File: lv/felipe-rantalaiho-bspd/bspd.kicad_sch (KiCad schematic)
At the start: 6 parts, among them J1 Conn_01x02, U4 L7805

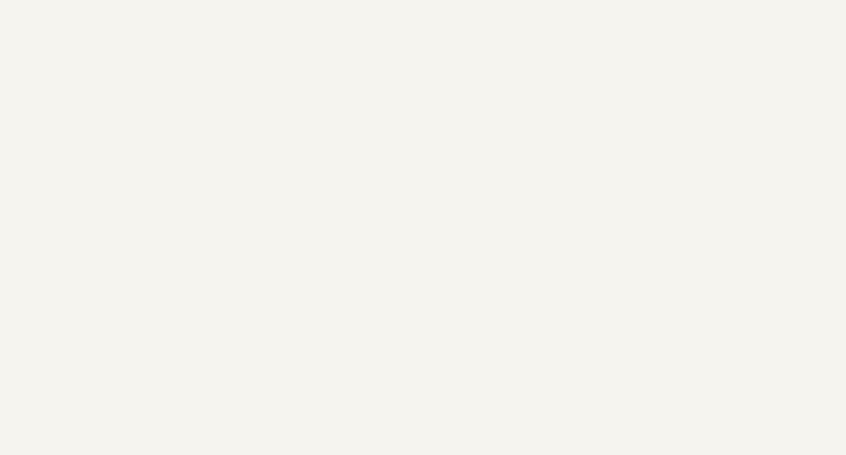
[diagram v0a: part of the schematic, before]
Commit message: Add block 2: brake pressure input + RC filter
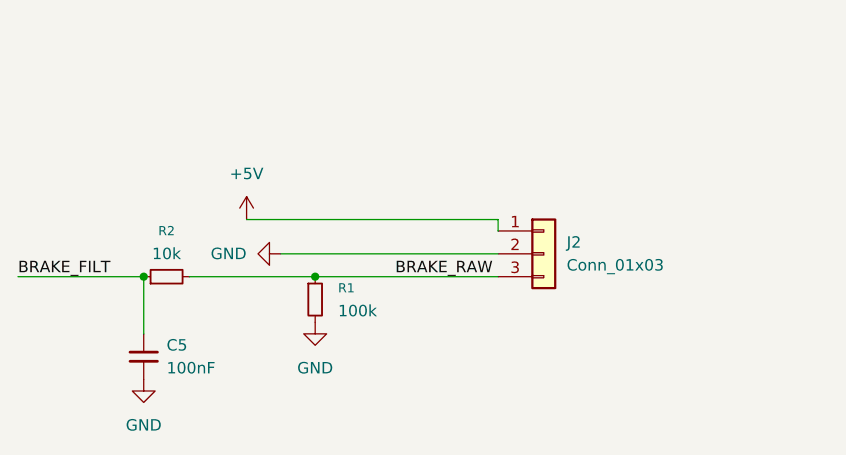
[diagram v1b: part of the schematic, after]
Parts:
- added C5: 100nF, Package_SO:SOIC-8_3.9x4.9mm_P1.27mm, symbol Device:C_Small
- added J2: Conn_01x03, Package_LCC:PLCC-84_29.3x29.3mm_P1.27mm, symbol Connector_Generic:Conn_01x03
- added R1: 100k, Package_DIP:DIP-8_W7.62mm, symbol Device:R_Small
- added R2: 10k, symbol Device:R_Small
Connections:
- net +5V: now also J2.1 (Pin_1)
- net GND: now also C5.2, J2.2 (Pin_2), R1.2
- new net BRAKE_FILT: C5.1, R2.1
- new net BRAKE_RAW: J2.3 (Pin_3), R1.1, R2.2

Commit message: Block Added
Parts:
- added C6: 100nF, symbol Device:C_Small
- added R3: 10k, Resistor_THT:R_Array_SIP4, symbol Device:R_Small
- added RV1: 10k, Display:ER_OLEDM0.91_1x-I2C, symbol Device:R_Potentiometer_Trim
- added U1: MCP6004, Package_DFN_QFN:QFN-20-1EP_5x5mm_P0.65mm_EP3.35x3.35mm, symbol Amplifier_Operational:MCP6004
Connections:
- net +5V: now also C6.1, R3.2, U1.4 (V+)
- net BRAKE_FILT: now also U1.3 (+)
- net GND: now also C6.2, RV1.3, U1.11 (V-)
- new net: R3.1, RV1.1
- new net BRAKE_HIGH: U1.1
- new net BRAKE_REF: RV1.2, U1.2 (-)
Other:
- moved on the sheet: C5, J2, R1, R2

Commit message: Add more  blocks
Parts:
- added C7, C8: 100nF, symbol Device:C_Small
- added J3: Conn_01x04, symbol Connector_Generic:Conn_01x04
- added R10, R11, R4, R5, R7: 10k, Resistor_THT:R_Array_SIP4, symbol Device:R_Small
- added R12: 13.7k, symbol Device:R_Small
- added R6, R8: 49.9k, symbol Device:R_Small
- added R9: 10k, symbol Device:R_Small
- added unit 3 of U1
- added unit 2 of U1
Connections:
- net +5V: now also J3.4 (Pin_4), R11.1
- net GND: now also C7.2, C8.2, J3.3 (Pin_3), R12.2, R4.2, R6.2
- new net: R5.1, R6.1, U1.5 (+)
- new net: R7.2, R8.2, U1.6 (-)
- new net CURRENT_REF: R11.2, R12.1, U1.9 (-)
- new net HASS_FILT: C8.1, R10.2
- new net HASS_OUT: J3.2 (Pin_2), R10.1, R4.1, R5.2
- new net HASS_REF: J3.1 (Pin_1), R7.1
- new net I_FILT: C7.1, R9.2, U1.10 (+)
- new net I_SCALED: R8.1, R9.1, U1.7
- new net POWER_HIGH: U1.8

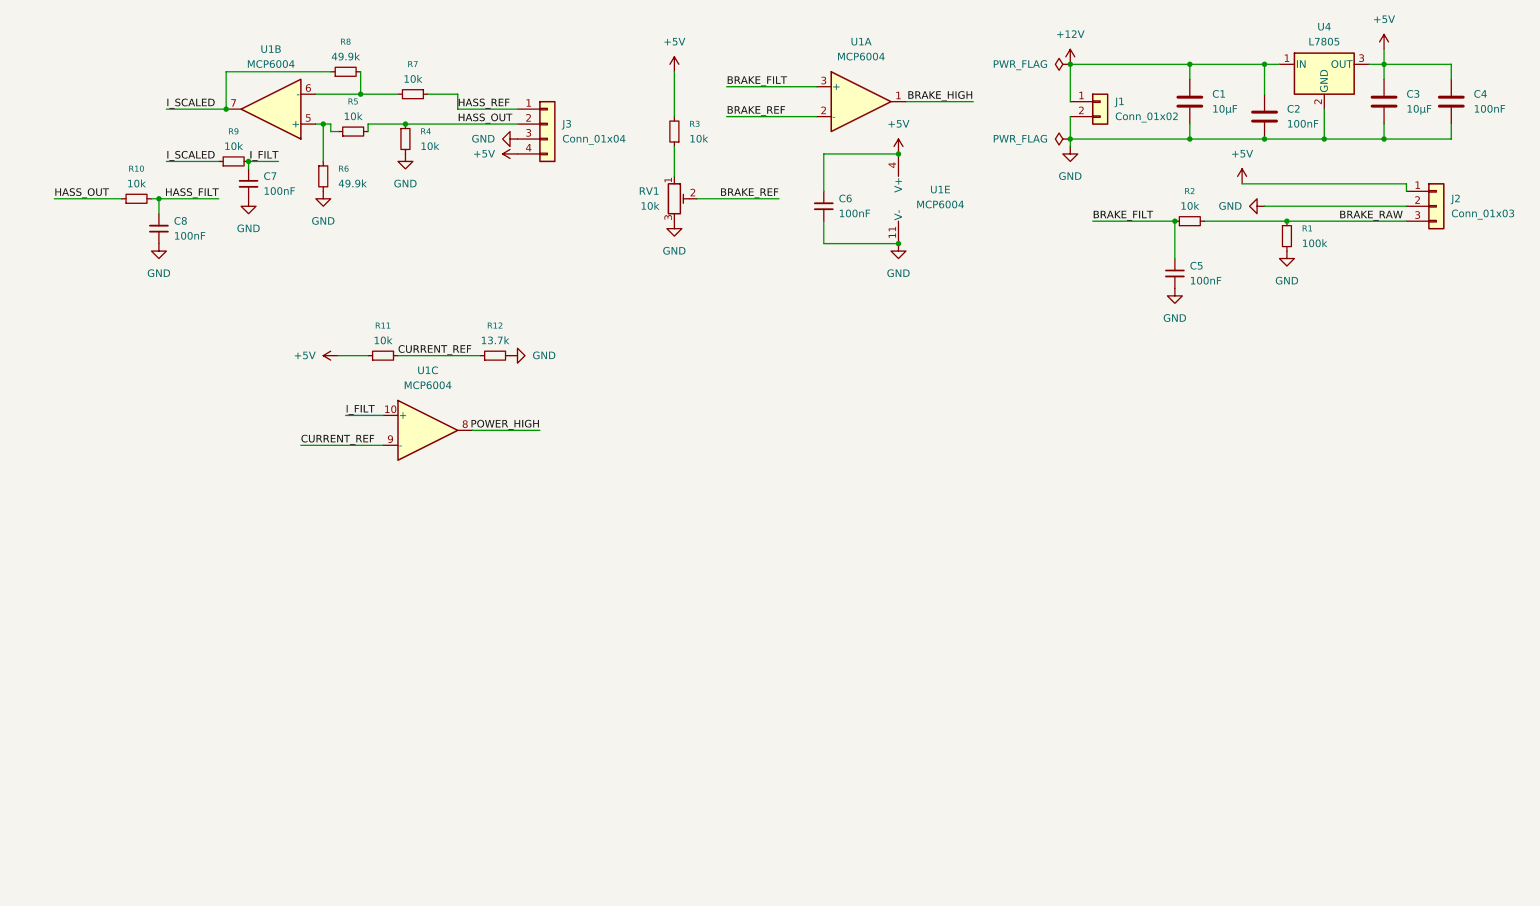
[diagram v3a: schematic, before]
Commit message: Add blocs: timer/latch and sensor fault detection
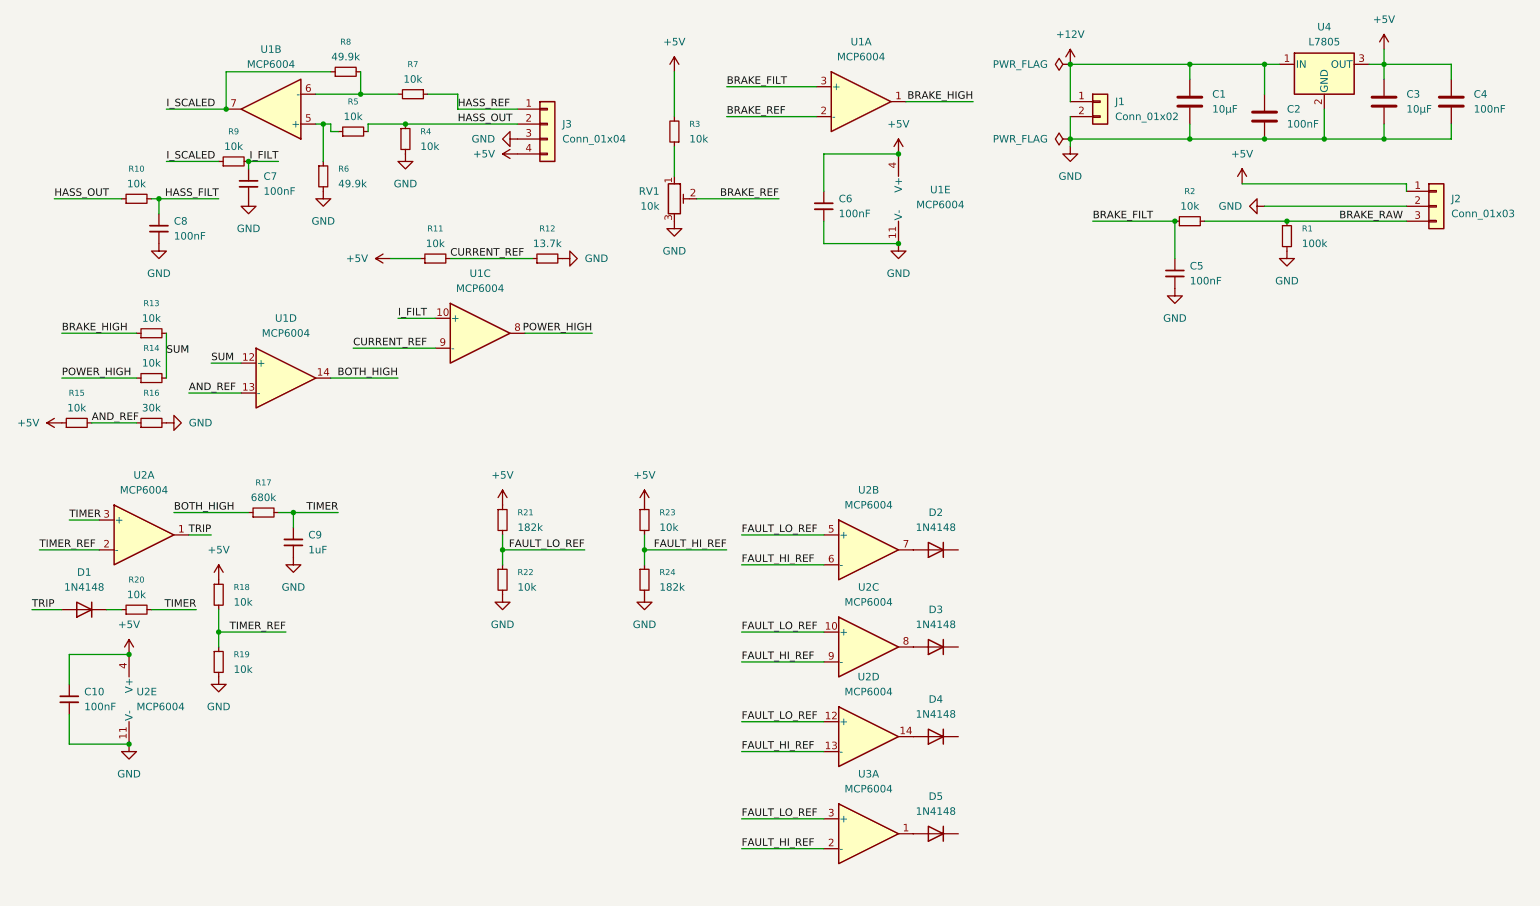
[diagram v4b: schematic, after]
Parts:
- added C10: 100nF, RF_Converter:Balun_Johanson_0900PC15J0013, symbol Device:C_Small
- added C9: 1uF, symbol Device:C_Small
- added D1, D2, D3, D4, D5: 1N4148, Diode_THT:D_DO-35_SOD27_P7.62mm_Horizontal, symbol Diode:1N4148
- added R13, R18: 10k, Resistor_THT:R_Array_SIP4, symbol Device:R_Small
- added R14, R15, R19, R22: 10k, symbol Device:R_Small
- added R16: 30k, symbol Device:R_Small
- added R17: 680k, Resistor_THT:R_Array_SIP4, symbol Device:R_Small
- added R20, R23: 10k, Diode_THT:D_DO-35_SOD27_P7.62mm_Horizontal, symbol Device:R_Small
- added R21: 182k, Diode_THT:D_DO-35_SOD27_P7.62mm_Horizontal, symbol Device:R_Small
- added R24: 182k, symbol Device:R_Small
- added unit 4 of U1
- added U2, U3: MCP6004, Package_DFN_QFN:QFN-20-1EP_5x5mm_P0.65mm_EP3.35x3.35mm, symbol Amplifier_Operational:MCP6004
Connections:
- net +5V: now also C10.1, R15.1, R18.1, R21.1, R23.1, U2.4 (V+)
- net BRAKE_HIGH: now also R13.1
- net GND: now also C10.2, C9.2, R16.2, R19.2, R22.2, R24.2, U2.11 (V-)
- net POWER_HIGH: now also R14.1
- new net: D1.1 (K), R20.1
- new net: D2.2 (A), U2.7
- new net: D5.2 (A), U3.1
- new net: D4.2 (A), U2.14
- new net: D3.2 (A), U2.8
- new net AND_REF: R15.2, R16.1, U1.13 (-)
- new net BOTH_HIGH: R17.1, U1.14
- new net FAULT_HI_REF: R23.2, R24.1, U2.13 (-), U2.6 (-), U2.9 (-), U3.2 (-)
- new net FAULT_LO_REF: R21.2, R22.1, U2.10 (+), U2.12 (+), U2.5 (+), U3.3 (+)
- new net SUM: R13.2, R14.2, U1.12 (+)
- new net TIMER: C9.1, R17.2, R20.2, U2.3 (+)
- new net TIMER_REF: R18.2, R19.1, U2.2 (-)
- new net TRIP: D1.2 (A), U2.1
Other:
- moved on the sheet: R11, R12, U1C

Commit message: Complete BSPD: output relay, test connector, title block
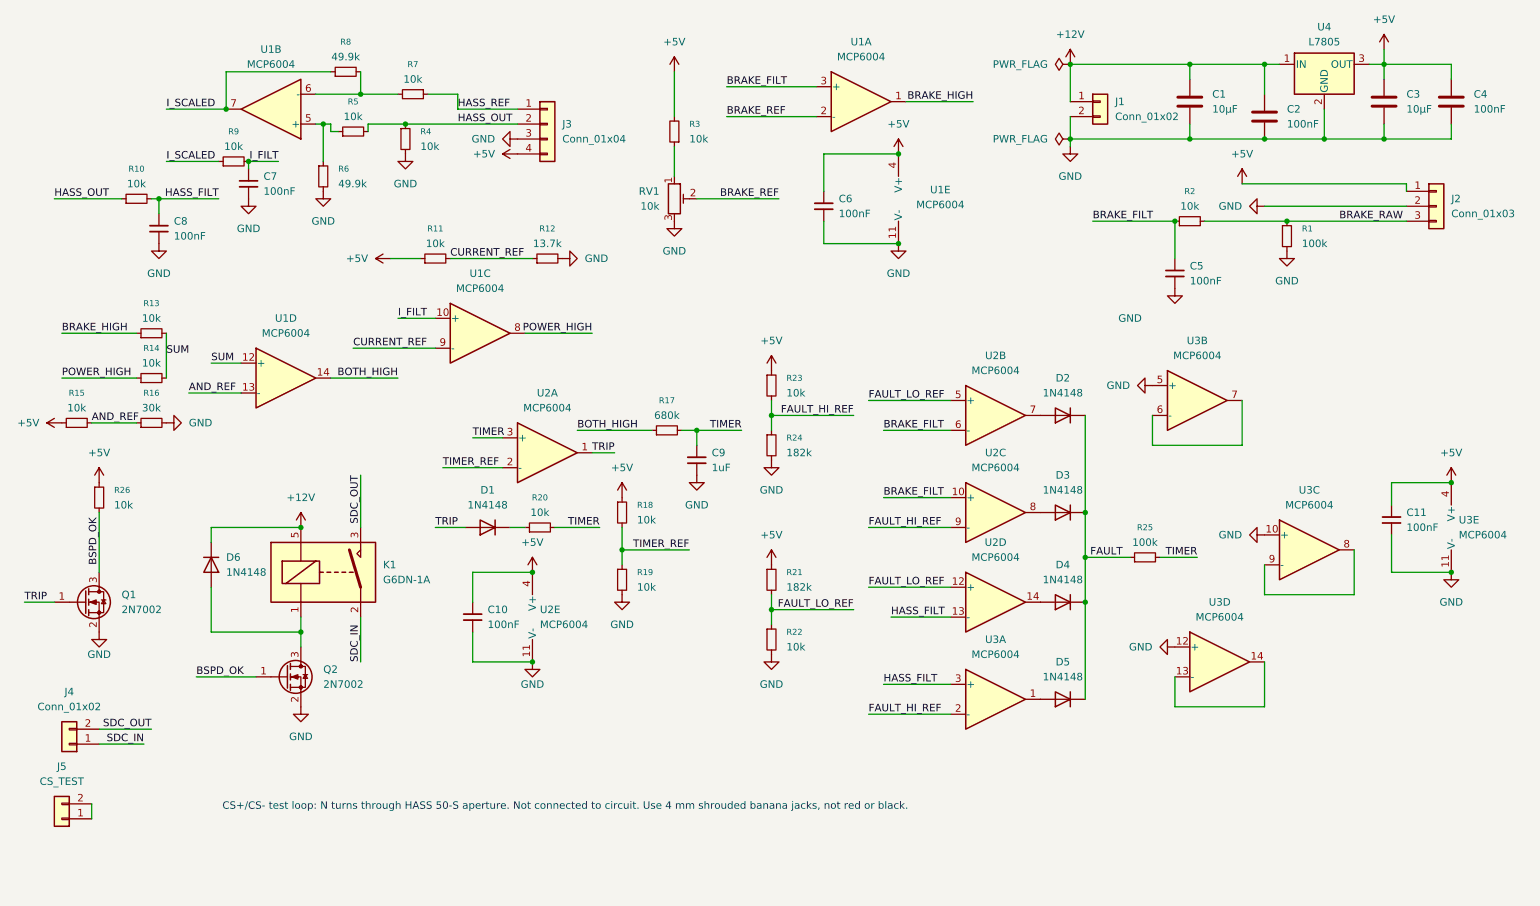
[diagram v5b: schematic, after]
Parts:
- added C11: 100nF, RF_Converter:Balun_Johanson_0900PC15J0013, symbol Device:C_Small
- added D6: 1N4148, Diode_THT:D_DO-35_SOD27_P7.62mm_Horizontal, symbol Diode:1N4148
- added J4: Conn_01x02, Relay_THT:Relay_SPST_Omron-G5Q-1A, symbol Connector_Generic:Conn_01x02
- added J5: CS_TEST, Relay_THT:Relay_SPST_Omron-G5Q-1A, symbol Connector_Generic:Conn_01x02
- added K1: G6DN-1A, Relay_THT:Relay_SPST_Omron-G5Q-1A, symbol Relay:G5Q-1A
- added Q1, Q2: 2N7002, Package_TO_SOT_SMD:SOT-23, symbol Transistor_FET:2N7002
- added R25: 100k, symbol Device:R_Small
- added R26: 10k, Package_TO_SOT_SMD:SOT-23, symbol Device:R_Small
- added unit 3 of U3
- added unit 2 of U3
- added unit 5 of U3
- added unit 4 of U3
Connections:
- net +12V: now also D6.1 (K), K1.5
- net +5V: now also C11.1, R26.1, U3.4 (V+)
- net BRAKE_FILT: now also U2.10 (+), U2.6 (-)
- net FAULT_HI_REF: no longer U2.13 (-), U2.6 (-)
- net FAULT_LO_REF: no longer U2.10 (+), U3.3 (+)
- net GND: now also C11.2, Q1.2 (S), Q2.2 (S), U3.10 (+), U3.11 (V-), U3.12 (+), U3.5 (+)
- net HASS_FILT: now also U2.13 (-), U3.3 (+)
- net TIMER: now also R25.2
- net TRIP: now also Q1.1 (G)
- net FAULT: now reaches D2.1 (K)
- net FAULT: now also D3.1 (K), D4.1 (K), D5.1 (K), R25.1
- new net: U3.8, U3.9 (-)
- new net: U3.6 (-), U3.7
- new net: D6.2 (A), K1.1, Q2.3 (D)
- new net: U3.13 (-), U3.14
- new net: J5.1 (Pin_1), J5.2 (Pin_2)
- new net BSPD_OK: Q1.3 (D), Q2.1 (G), R26.2
- new net SDC_IN: J4.1 (Pin_1), K1.2
- new net SDC_OUT: J4.2 (Pin_2), K1.3
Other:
- note added: "CS+/CS- test loop: N turns through HASS 50-S aperture. Not connected to circuit. Use 4 mm shrouded banana jacks, not red or black."
- title: ${BOARD_TITLE} -> BSPD
- moved on the sheet: C10, C9, D1, D2, D3, D4, D5, R17, R18, R19, R20, R21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

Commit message: BSPD: Uref fault check, 42 A threshold, 0.33 s timer, C9 discharge diode, calculations and writeup from google docs
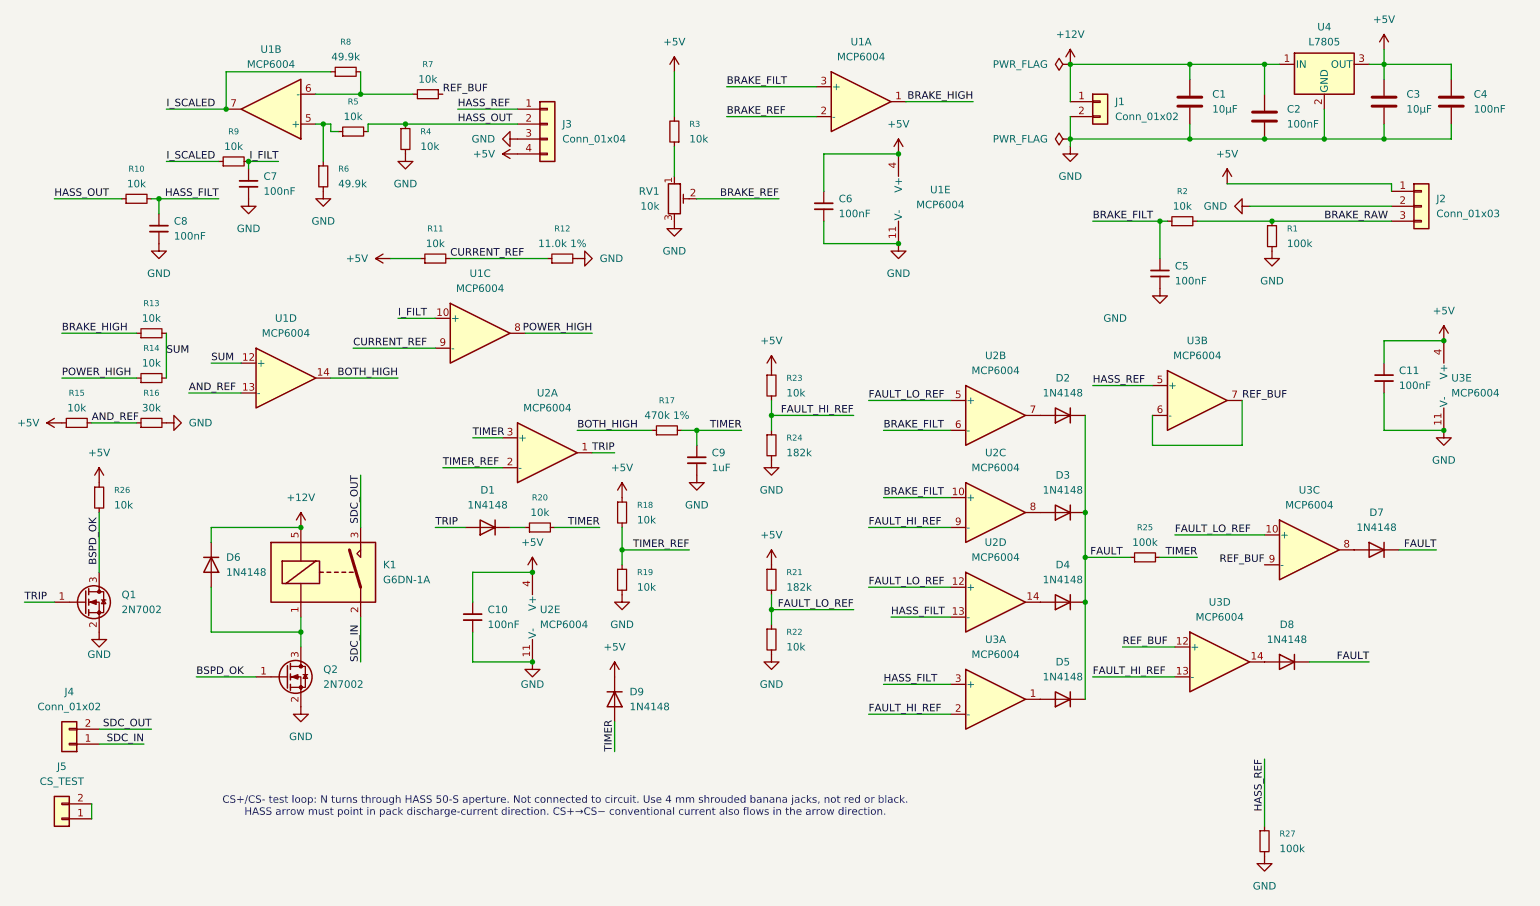
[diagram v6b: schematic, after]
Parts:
- added D7, D8, D9: 1N4148, Diode_THT:D_DO-35_SOD27_P7.62mm_Horizontal, symbol Diode:1N4148
- added R27: 100k, Package_TO_SOT_SMD:SOT-23, symbol Device:R_Small
- R12: value 13.7k -> 11.0k 1%
- R17: value 680k -> 470k 1%
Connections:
- net +5V: now also D9.1 (K)
- net FAULT: now also D7.1 (K), D8.1 (K)
- net FAULT_HI_REF: now also U3.13 (-)
- net FAULT_LO_REF: now also U3.10 (+)
- net GND: now also R27.2; no longer U3.10 (+), U3.12 (+), U3.5 (+)
- net HASS_REF: now also U3.5 (+), R27.1; no longer R7.1
- net TIMER: now also D9.2 (A)
- net at U3.8: now also D7.2 (A); no longer U3.9 (-)
- net REF_BUF: now reaches U3.6 (-), U3.7
- net REF_BUF: now also R7.1, U3.12 (+), U3.9 (-)
- net at U3.14: now also D8.2 (A); no longer U3.13 (-)
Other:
- note added: "CS+/CS- test loop: N turns through HASS 50-S aperture. Not connected to circuit. Use 4 mm shrouded banana jacks, not red or black. HASS arrow must point in pack discharge-current direction. CS+→CS− conventional current also flows in the arrow direction."
- note removed: "CS+/CS- test loop: N turns through HASS 50-S aperture. Not connected to circuit. Use 4 mm shrouded banana jacks, not red or black."
- moved on the sheet: C11, C5, J2, R1, R12, R2, R7, U3E
